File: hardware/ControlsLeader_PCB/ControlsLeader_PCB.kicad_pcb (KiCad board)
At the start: 2 copper layers, 42 parts, among them J1 CarCANConnector_Out, J15 IgnConn_01x04, J16 SteeringConn_01x05, J17 Conn_01x02, J2 PeripheralCAN_out, J3 CarCANConnector_In, J4 PeripheralCAN_in, J6 DashConn1_2Rows-09Pins, J7 Dash_LSOM_PWR, J8 DashConn2_2Rows-09Pins, Q14 NMOS, Q6 NMOS, Q9 NMOS, U2 LeaderSOM, U4 LT1963AEST-3.3#TRPBF, U6 TPS5405DR

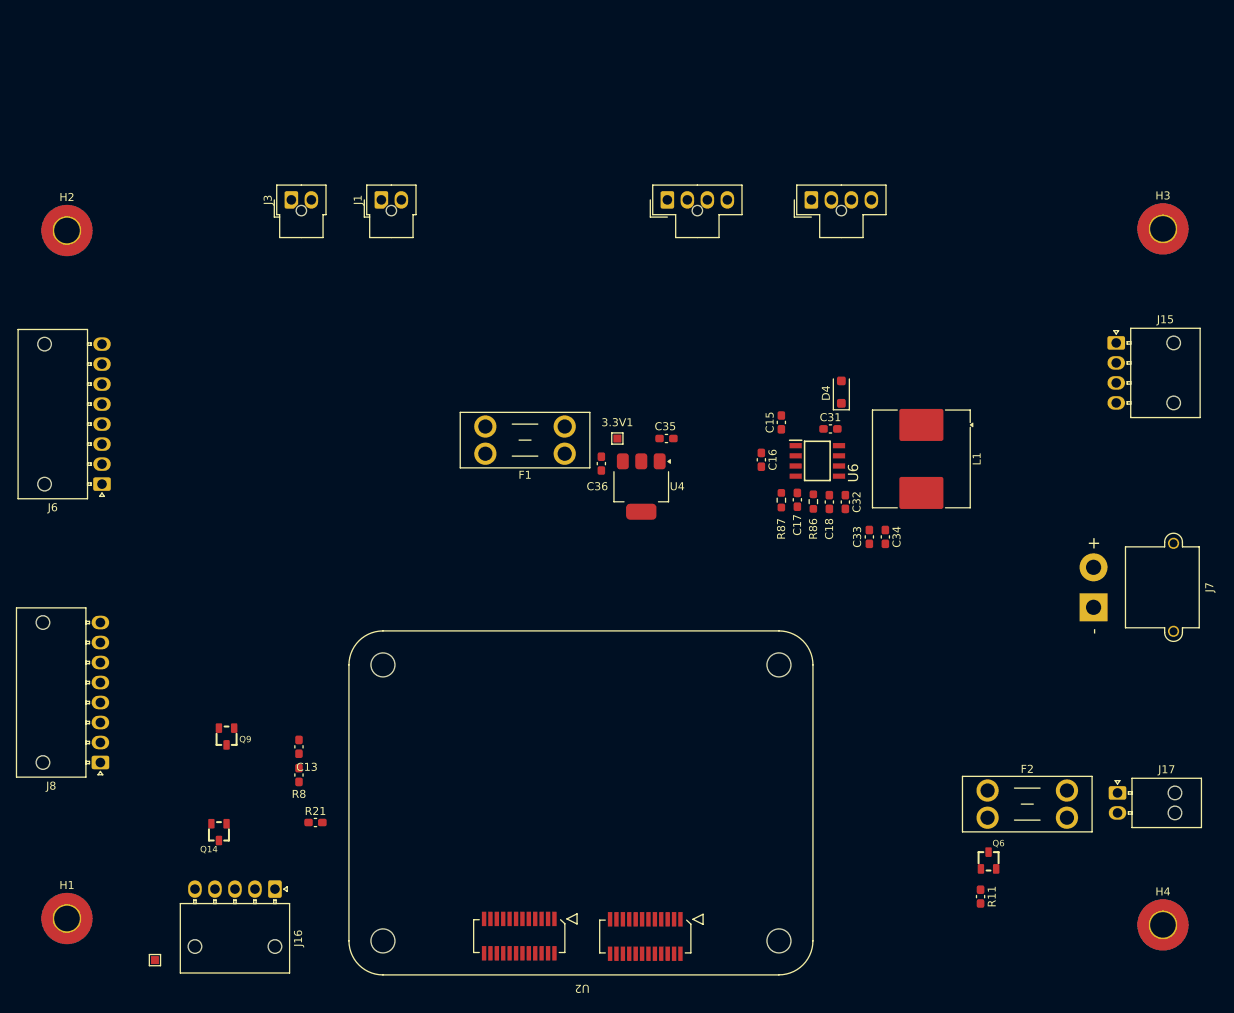
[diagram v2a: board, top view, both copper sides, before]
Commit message: PCB DESIGN DONE - need to add datasheets and p/n
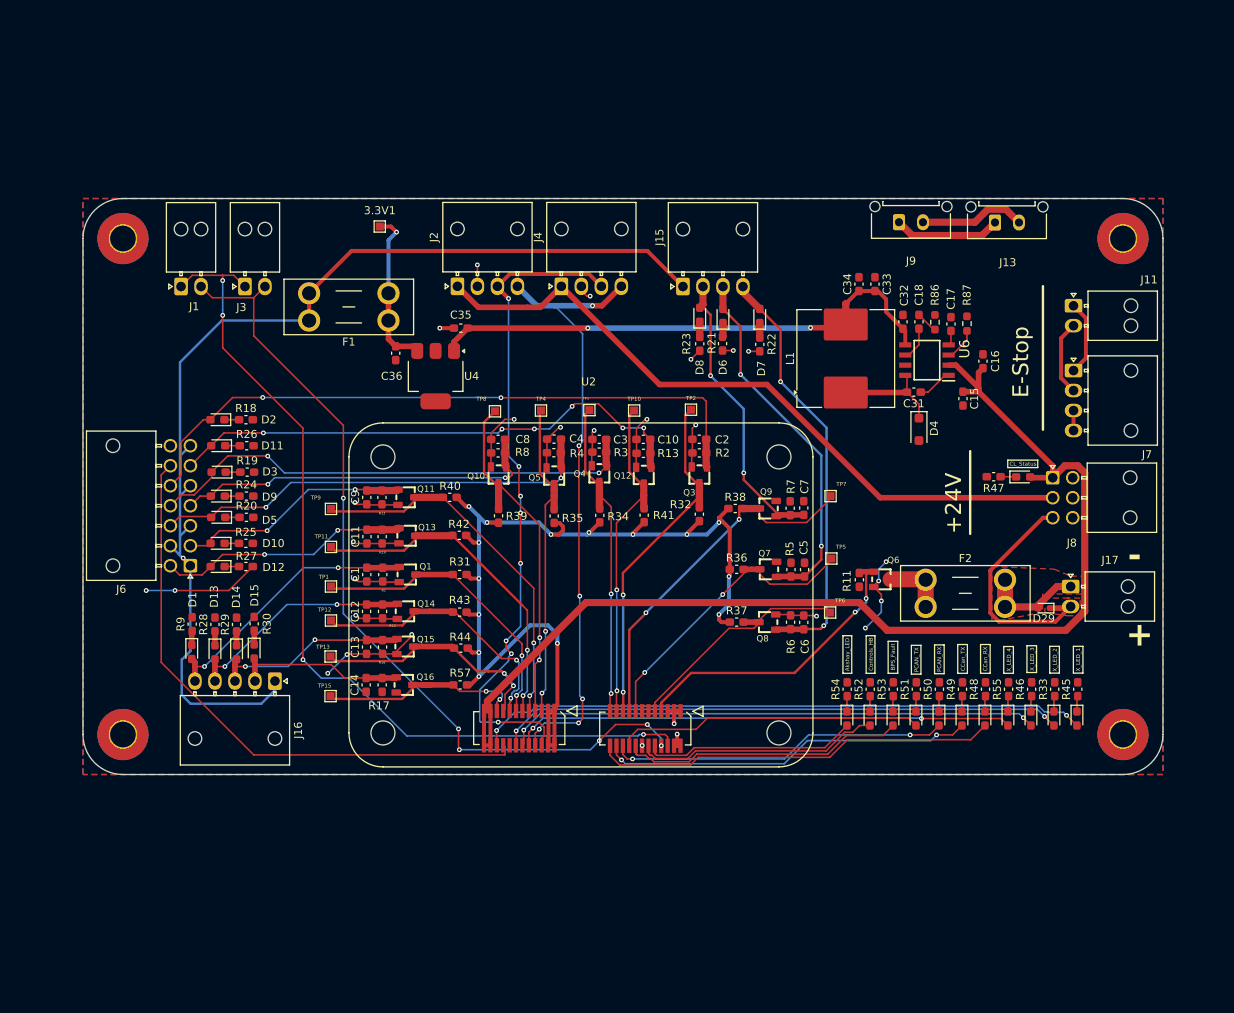
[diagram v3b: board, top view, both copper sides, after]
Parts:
- added C1: 5uF, Capacitor_SMD:C_0603_1608Metric_Pad1.08x0.95mm_HandSolder, F.Cu at (120.5, 105.0)
- added C10: 5uF, Capacitor_SMD:C_0603_1608Metric_Pad1.08x0.95mm_HandSolder, F.Cu at (155.1, 88.1)
- added C11: 5uF, Capacitor_SMD:C_0603_1608Metric_Pad1.08x0.95mm_HandSolder, F.Cu at (120.5, 100.3)
- added C12: 5uF, Capacitor_SMD:C_0603_1608Metric_Pad1.08x0.95mm_HandSolder, F.Cu at (120.5, 109.6)
- added C14: 5uF, Capacitor_SMD:C_0603_1608Metric_Pad1.08x0.95mm_HandSolder, F.Cu at (120.4, 118.8)
- added C2: 5uF, Capacitor_SMD:C_0603_1608Metric_Pad1.08x0.95mm_HandSolder, F.Cu at (162.0, 88.1)
- added C3: 5uF, Capacitor_SMD:C_0603_1608Metric_Pad1.08x0.95mm_HandSolder, F.Cu at (149.5, 88.1)
- added C4: 5uF, Capacitor_SMD:C_0603_1608Metric_Pad1.08x0.95mm_HandSolder, F.Cu at (143.9, 88.1)
- added C5: 5uF, Capacitor_SMD:C_0603_1608Metric_Pad1.08x0.95mm_HandSolder, F.Cu at (175.2, 104.4)
- added C6: 5uF, Capacitor_SMD:C_0603_1608Metric_Pad1.08x0.95mm_HandSolder, F.Cu at (175.1, 111.0)
- added C7: 5uF, Capacitor_SMD:C_0603_1608Metric_Pad1.08x0.95mm_HandSolder, F.Cu at (175.1, 96.7)
- added C8: 5uF, Capacitor_SMD:C_0603_1608Metric_Pad1.08x0.95mm_HandSolder, F.Cu at (136.9, 88.1)
- added C9: 5uF, Capacitor_SMD:C_0603_1608Metric_Pad1.08x0.95mm_HandSolder, F.Cu at (120.5, 95.4)
- added D1: GPIO_Status_Blue, LED_SMD:LED_0603_1608Metric_Pad1.05x0.95mm_HandSolder, F.Cu at (98.6, 114.7)
- added D10: GPIO_Status_Blue, LED_SMD:LED_0603_1608Metric_Pad1.05x0.95mm_HandSolder, F.Cu at (101.8, 101.1)
- added D11: GPIO_Status_Blue, LED_SMD:LED_0603_1608Metric_Pad1.05x0.95mm_HandSolder, F.Cu at (101.9, 88.9)
- added D12: GPIO_Status_Blue, LED_SMD:LED_0603_1608Metric_Pad1.05x0.95mm_HandSolder, F.Cu at (101.8, 104.0)
- added D13: GPIO_Status_Blue, LED_SMD:LED_0603_1608Metric_Pad1.05x0.95mm_HandSolder, F.Cu at (101.5, 114.7)
- added D14: GPIO_Status_Blue, LED_SMD:LED_0603_1608Metric_Pad1.05x0.95mm_HandSolder, F.Cu at (104.2, 114.7)
- added D15: GPIO_Status_Blue, LED_SMD:LED_0603_1608Metric_Pad1.05x0.95mm_HandSolder, F.Cu at (106.4, 114.6)
- added D16: Controls_Leader_Status_Red, LED_SMD:LED_0603_1608Metric_Pad1.05x0.95mm_HandSolder, F.Cu at (202.5, 92.8)
- added D17: 0603_SMD, LED_SMD:LED_0603_1608Metric_Pad1.05x0.95mm_HandSolder, F.Cu at (209.2, 123.0)
- added D18: 0603_SMD, LED_SMD:LED_0603_1608Metric_Pad1.05x0.95mm_HandSolder, F.Cu at (206.4, 123.0)
- added D19: 0603_SMD, LED_SMD:LED_0603_1608Metric_Pad1.05x0.95mm_HandSolder, F.Cu at (197.8, 123.0)
- added D2: GPIO_Status_Blue, LED_SMD:LED_0603_1608Metric_Pad1.05x0.95mm_HandSolder, F.Cu at (101.8, 85.7)
- added D20: 0603_SMD, LED_SMD:LED_0603_1608Metric_Pad1.05x0.95mm_HandSolder, F.Cu at (194.9, 123.0)
- added D21: 0603_SMD, LED_SMD:LED_0603_1608Metric_Pad1.05x0.95mm_HandSolder, F.Cu at (192.0, 123.0)
- added D22: 0603_SMD, LED_SMD:LED_0603_1608Metric_Pad1.05x0.95mm_HandSolder, F.Cu at (189.1, 123.0)
- added D23: 0603_SMD, LED_SMD:LED_0603_1608Metric_Pad1.05x0.95mm_HandSolder, F.Cu at (183.4, 123.0)
- added D24: 0603_SMD, LED_SMD:LED_0603_1608Metric_Pad1.05x0.95mm_HandSolder, F.Cu at (186.2, 123.0)
- added D25: 0603_SMD, LED_SMD:LED_0603_1608Metric_Pad1.05x0.95mm_HandSolder, F.Cu at (180.5, 123.0)
- added D26: 0603_SMD, LED_SMD:LED_0603_1608Metric_Pad1.05x0.95mm_HandSolder, F.Cu at (203.5, 123.0)
- added D27: 0603_SMD, LED_SMD:LED_0603_1608Metric_Pad1.05x0.95mm_HandSolder, F.Cu at (200.6, 123.0)
- added D29: VSSAF522-M3/H, Diode_SMD:D_SOD-523, F.Cu at (205.1, 109.2)
- added D3: GPIO_Status_Blue, LED_SMD:LED_0603_1608Metric_Pad1.05x0.95mm_HandSolder, F.Cu at (102.0, 92.2)
- added D5: GPIO_Status_Blue, LED_SMD:LED_0603_1608Metric_Pad1.05x0.95mm_HandSolder, F.Cu at (101.9, 97.8)
- added D6: GPIO_Status_Blue, LED_SMD:LED_0603_1608Metric_Pad1.05x0.95mm_HandSolder, F.Cu at (165.0, 72.7)
- added D7: GPIO_Status_Blue, LED_SMD:LED_0603_1608Metric_Pad1.05x0.95mm_HandSolder, F.Cu at (169.6, 72.7)
- added D8: GPIO_Status_Blue, LED_SMD:LED_0603_1608Metric_Pad1.05x0.95mm_HandSolder, F.Cu at (162.1, 72.5)
- added D9: GPIO_Status_Blue, LED_SMD:LED_0603_1608Metric_Pad1.05x0.95mm_HandSolder, F.Cu at (101.9, 95.2)
- added J11: EStop1, Connector_Molex:Molex_Nano-Fit_105313-xx02_1x02_P2.50mm_Horizontal, F.Cu at (208.8, 71.4)
- added J13: Supp_Out, Connector_Molex:Molex_Micro-Fit_3.0_43650-0215_1x02_P3.00mm_Vertical, F.Cu at (199.0, 61.0)
- added J9: Supp_In, Connector_Molex:Molex_Micro-Fit_3.0_43650-0215_1x02_P3.00mm_Vertical, F.Cu at (187.0, 61.0)
- added Q1: NMOS, LSOM_IRLM:SOT23, F.Cu at (124.5, 104.0)
- added Q10: NMOS, LSOM_IRLM:SOT23, F.Cu at (137.9, 91.5)
- added Q11: NMOS, LSOM_IRLM:SOT23, F.Cu at (124.4, 94.4)
- added Q12: NMOS, LSOM_IRLM:SOT23, F.Cu at (156.1, 91.6)
- added Q13: NMOS, LSOM_IRLM:SOT23, F.Cu at (124.5, 99.2)
- added Q15: NMOS, LSOM_IRLM:SOT23, F.Cu at (124.2, 113.0)
- added Q16: NMOS, LSOM_IRLM:SOT23, F.Cu at (124.2, 117.8)
- added Q3: NMOS, LSOM_IRLM:SOT23, F.Cu at (163.0, 91.5)
- added Q4: NMOS, LSOM_IRLM:SOT23, F.Cu at (150.5, 91.4)
- added Q5: NMOS, LSOM_IRLM:SOT23, F.Cu at (144.8, 91.7)
- added Q7: NMOS, LSOM_IRLM:SOT23, F.Cu at (171.7, 105.3)
- added Q8: NMOS, LSOM_IRLM:SOT23, F.Cu at (171.6, 111.9)
- added R1: 10k, Capacitor_SMD:C_0603_1608Metric_Pad1.08x0.95mm_HandSolder, F.Cu at (122.5, 105.0)
- added R12: 10k, Capacitor_SMD:C_0603_1608Metric_Pad1.08x0.95mm_HandSolder, F.Cu at (122.4, 95.4)
- added R13: 10k, Capacitor_SMD:C_0603_1608Metric_Pad1.08x0.95mm_HandSolder, F.Cu at (155.1, 89.8)
- added R14: 10k, Capacitor_SMD:C_0603_1608Metric_Pad1.08x0.95mm_HandSolder, F.Cu at (122.4, 100.3)
- added R15: 10k, Capacitor_SMD:C_0603_1608Metric_Pad1.08x0.95mm_HandSolder, F.Cu at (122.5, 109.6)
- added R16: 10k, Capacitor_SMD:C_0603_1608Metric_Pad1.08x0.95mm_HandSolder, F.Cu at (122.5, 114.1)
- added R17: 10k, Capacitor_SMD:C_0603_1608Metric_Pad1.08x0.95mm_HandSolder, F.Cu at (122.4, 118.8)
- added R18: 150, Capacitor_SMD:C_0603_1608Metric_Pad1.08x0.95mm_HandSolder, F.Cu at (105.4, 85.7)
- added R19: 150, Capacitor_SMD:C_0603_1608Metric_Pad1.08x0.95mm_HandSolder, F.Cu at (105.5, 92.2)
- added R2: 10k, Capacitor_SMD:C_0603_1608Metric_Pad1.08x0.95mm_HandSolder, F.Cu at (162.1, 89.8)
- added R20: 150, Capacitor_SMD:C_0603_1608Metric_Pad1.08x0.95mm_HandSolder, F.Cu at (105.4, 97.8)
- added R22: 150, Capacitor_SMD:C_0603_1608Metric_Pad1.08x0.95mm_HandSolder, F.Cu at (169.6, 76.2)
- added R23: 150, Capacitor_SMD:C_0603_1608Metric_Pad1.08x0.95mm_HandSolder, F.Cu at (162.1, 76.2)
- added R24: 150, Capacitor_SMD:C_0603_1608Metric_Pad1.08x0.95mm_HandSolder, F.Cu at (105.4, 95.2)
- added R25: 150, Capacitor_SMD:C_0603_1608Metric_Pad1.08x0.95mm_HandSolder, F.Cu at (105.4, 101.1)
- added R26: 150, Capacitor_SMD:C_0603_1608Metric_Pad1.08x0.95mm_HandSolder, F.Cu at (105.5, 88.9)
- added R27: 150, Capacitor_SMD:C_0603_1608Metric_Pad1.08x0.95mm_HandSolder, F.Cu at (105.4, 104.0)
- added R28: 150, Capacitor_SMD:C_0603_1608Metric_Pad1.08x0.95mm_HandSolder, F.Cu at (101.5, 111.2)
- added R29: 150, Capacitor_SMD:C_0603_1608Metric_Pad1.08x0.95mm_HandSolder, F.Cu at (104.2, 111.2)
- added R3: 10k, Capacitor_SMD:C_0603_1608Metric_Pad1.08x0.95mm_HandSolder, F.Cu at (149.5, 89.7)
- added R30: 150, Capacitor_SMD:C_0603_1608Metric_Pad1.08x0.95mm_HandSolder, F.Cu at (106.4, 111.2)
- added R31: 100k, Capacitor_SMD:C_0603_1608Metric_Pad1.08x0.95mm_HandSolder, F.Cu at (132.1, 105.0)
- added R32: 100k, Capacitor_SMD:C_0603_1608Metric_Pad1.08x0.95mm_HandSolder, F.Cu at (162.1, 97.5)
- added R33: 65, Capacitor_SMD:C_0603_1608Metric_Pad1.08x0.95mm_HandSolder, F.Cu at (206.5, 119.3)
- added R34: 100k, Capacitor_SMD:C_0603_1608Metric_Pad1.08x0.95mm_HandSolder, F.Cu at (149.6, 97.6)
- added R35: 100k, Capacitor_SMD:C_0603_1608Metric_Pad1.08x0.95mm_HandSolder, F.Cu at (143.9, 97.7)
- added R36: 100k, Capacitor_SMD:C_0603_1608Metric_Pad1.08x0.95mm_HandSolder, F.Cu at (166.7, 104.3)
- added R37: 100k, Capacitor_SMD:C_0603_1608Metric_Pad1.08x0.95mm_HandSolder, F.Cu at (166.7, 111.0)
- added R38: 100k, Capacitor_SMD:C_0603_1608Metric_Pad1.08x0.95mm_HandSolder, F.Cu at (166.5, 96.8)
- added R39: 100k, Capacitor_SMD:C_0603_1608Metric_Pad1.08x0.95mm_HandSolder, F.Cu at (136.9, 97.7)
- added R4: 10k, Capacitor_SMD:C_0603_1608Metric_Pad1.08x0.95mm_HandSolder, F.Cu at (143.9, 89.8)
- added R40: 100k, Capacitor_SMD:C_0603_1608Metric_Pad1.08x0.95mm_HandSolder, F.Cu at (130.8, 95.3)
- added R41: 100k, Capacitor_SMD:C_0603_1608Metric_Pad1.08x0.95mm_HandSolder, F.Cu at (155.2, 97.6)
- added R42: 100k, Capacitor_SMD:C_0603_1608Metric_Pad1.08x0.95mm_HandSolder, F.Cu at (132.0, 100.1)
- added R43: 100k, Capacitor_SMD:C_0603_1608Metric_Pad1.08x0.95mm_HandSolder, F.Cu at (132.1, 109.7)
- added R44: 100k, Capacitor_SMD:C_0603_1608Metric_Pad1.08x0.95mm_HandSolder, F.Cu at (132.2, 114.2)
- added R45: 65, Capacitor_SMD:C_0603_1608Metric_Pad1.08x0.95mm_HandSolder, F.Cu at (209.3, 119.3)
- added R46: 65, Capacitor_SMD:C_0603_1608Metric_Pad1.08x0.95mm_HandSolder, F.Cu at (203.6, 119.3)
- added R47: 1.1k, Capacitor_SMD:C_0603_1608Metric_Pad1.08x0.95mm_HandSolder, F.Cu at (198.8, 92.8)
- added R48: 20, Capacitor_SMD:C_0603_1608Metric_Pad1.08x0.95mm_HandSolder, F.Cu at (197.8, 119.3)
- added R49: 20, Capacitor_SMD:C_0603_1608Metric_Pad1.08x0.95mm_HandSolder, F.Cu at (194.9, 119.3)
- added R5: 10k, Capacitor_SMD:C_0603_1608Metric_Pad1.08x0.95mm_HandSolder, F.Cu at (173.5, 104.4)
- added R50: 20, Capacitor_SMD:C_0603_1608Metric_Pad1.08x0.95mm_HandSolder, F.Cu at (192.1, 119.3)
- added R51: 20, Capacitor_SMD:C_0603_1608Metric_Pad1.08x0.95mm_HandSolder, F.Cu at (189.2, 119.3)
- added R52: 20, Capacitor_SMD:C_0603_1608Metric_Pad1.08x0.95mm_HandSolder, F.Cu at (183.4, 119.3)
- added R53: 20, Capacitor_SMD:C_0603_1608Metric_Pad1.08x0.95mm_HandSolder, F.Cu at (186.3, 119.3)
- added R54: 20, Capacitor_SMD:C_0603_1608Metric_Pad1.08x0.95mm_HandSolder, F.Cu at (180.5, 119.3)
- added R55: 65, Capacitor_SMD:C_0603_1608Metric_Pad1.08x0.95mm_HandSolder, F.Cu at (200.7, 119.3)
- added R57: 100k, Capacitor_SMD:C_0603_1608Metric_Pad1.08x0.95mm_HandSolder, F.Cu at (132.2, 118.8)
- added R6: 10k, Capacitor_SMD:C_0603_1608Metric_Pad1.08x0.95mm_HandSolder, F.Cu at (173.4, 111.0)
- added R7: 10k, Capacitor_SMD:C_0603_1608Metric_Pad1.08x0.95mm_HandSolder, F.Cu at (173.4, 96.7)
- added R9: 150, Capacitor_SMD:C_0603_1608Metric_Pad1.08x0.95mm_HandSolder, F.Cu at (98.7, 111.2)
- added TP1: TestPoint, TestPoint:TestPoint_Pad_1.0x1.0mm, F.Cu at (116.0, 106.5)
- added TP10: TestPoint, TestPoint:TestPoint_Pad_1.0x1.0mm, F.Cu at (153.9, 84.5)
- added TP11: TestPoint, TestPoint:TestPoint_Pad_1.0x1.0mm, F.Cu at (116.0, 101.5)
- added TP12: TestPoint, TestPoint:TestPoint_Pad_1.0x1.0mm, F.Cu at (116.0, 110.8)
- added TP15: TestPoint, TestPoint:TestPoint_Pad_1.0x1.0mm, F.Cu at (116.0, 120.2)
- added TP2: TestPoint, TestPoint:TestPoint_Pad_1.0x1.0mm, F.Cu at (161.0, 84.4)
- added TP3: TestPoint, TestPoint:TestPoint_Pad_1.0x1.0mm, F.Cu at (148.3, 84.5)
- added TP4: TestPoint, TestPoint:TestPoint_Pad_1.0x1.0mm, F.Cu at (142.2, 84.5)
- added TP5: TestPoint, TestPoint:TestPoint_Pad_1.0x1.0mm, F.Cu at (178.6, 103.0)
- added TP6: TestPoint, TestPoint:TestPoint_Pad_1.0x1.0mm, F.Cu at (178.4, 109.8)
- added TP7: TestPoint, TestPoint:TestPoint_Pad_1.0x1.0mm, F.Cu at (178.4, 95.2)
- added TP8: TestPoint, TestPoint:TestPoint_Pad_1.0x1.0mm, F.Cu at (136.5, 84.6)
- added TP9: TestPoint, TestPoint:TestPoint_Pad_1.0x1.0mm, F.Cu at (116.0, 96.8)
- J1, J3: footprint UTSVT_Connectors:Molex_Nano-Fit_105309-xx02_1x02_P2.50mm_Vertical -> Connector_Molex:Molex_Nano-Fit_105313-xx02_1x02_P2.50mm_Horizontal
- J2, J4: footprint UTSVT_Connectors:Molex_Nano-Fit_105309-xx04_1x04_P2.50mm_Vertical -> Connector_Molex:Molex_Nano-Fit_105313-xx04_1x04_P2.50mm_Horizontal
- J6: value DashConn1_2Rows-09Pins -> Conn_2Rows-13Pins; footprint Connector_Molex:Molex_Nano-Fit_105313-xx08_1x08_P2.50mm_Horizontal -> Connector_Molex:Molex_Nano-Fit_105314-xx14_2x07_P2.50mm_Horizontal
- J7: value Dash_LSOM_PWR -> Conn_01x04; footprint UTSVT_Connectors:AMASS_XT30PW-M_1x02_P2.50mm_Horizontal -> Connector_Molex:Molex_Nano-Fit_105313-xx04_1x04_P2.50mm_Horizontal
- J8: value DashConn2_2Rows-09Pins -> Dash_Lsom_Horn_Lights_PWR; footprint Connector_Molex:Molex_Nano-Fit_105313-xx08_1x08_P2.50mm_Horizontal -> Connector_Molex:Molex_Nano-Fit_105314-xx06_2x03_P2.50mm_Horizontal
- moved H4 132.2 mm to (90.0, 125.0)
- moved H2 132.0 mm to (215.0, 63.0)
- moved J8 124.2 mm to (206.2, 92.9), turned to 0 degrees
- moved H1 85.3 mm to (90.0, 63.0)
- moved R21 78.6 mm to (164.9, 76.1), turned to -90 degrees
- moved Q9 72.7 mm to (171.7, 97.7), turned to 90 degrees
- moved H3 63.4 mm to (215.0, 125.0)
- moved J15 54.6 mm to (160.0, 69.0), turned to 90 degrees
- moved J2 48.5 mm to (131.8, 69.0)
- moved R8 47.3 mm to (136.9, 89.8), turned to 0 degrees
- moved TP13 43.8 mm to (116.0, 115.2)
- moved R11 42.4 mm to (182.1, 105.7)
- moved 3.3V1 39.8 mm to (122.1, 61.5)
- moved Q6 39.5 mm to (183.8, 104.7), turned to -90 degrees
- moved Q14 34.8 mm to (124.3, 108.7), turned to -90 degrees
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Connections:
- C13 pad 2: /Steering_Wheel/NMOS Switch1/3.3V_LDO_Switch -> /Right_Blinker_Signal
- J15 pad 2: /Ign_mtr_GPIO -> /Ign_mtr_Signal
- J15 pad 3: /Ign_OFF_GPIO -> /Ign_off_Signal
- J15 pad 4: /Ign_arr_GPIO -> /Ign_arr_Signal
- J16 pad 2: /Left_Blinker_ON -> /Left_Blinker_Signal
- J16 pad 3: /Right_Blinker_ON -> /Right_Blinker_Signal
- J16 pad 4: /Horn_GPIO_IN -> /Horn_3.3V_Signal
- J16 pad 5: /Regen_Active_GPIO_IN -> /Regen_Active_Signal
- J17 pad 2: unconnected-(J17-Pin_2-Pad2) -> /+24v_Horn
- J2 pad 1: +24V -> /+24v_Lights
- J4 pad 1: +24V -> /+24v_Lights
- J6 pad 2: /Rev_SW_GPIO -> /Cruise_Set_Signal
- J6 pad 4: /Fwd_SW_GPIO -> /Cruise_Enable_Signal
- J6 pad 6: /Neutral_Gear_GPIO -> /Regen_Enable_Signal
- J6 pad 8: unconnected-(J6-Pin_8-Pad8) -> /Hazard_Signal
- J7 pad 1: +24V -> /Dash/Contactor_OUT1
- J7 pad 2: GND -> /Dash/Contactor_IN1
- J8 pad 1: /3.3V_LDO -> +24V
- J8 pad 2: /Cruise_Set_GPIO_IN -> /+24v_Lights
- J8 pad 3: /3.3V_LDO -> /+24v_Horn
- J8 pad 4: /Cruise_Enable_GPIO_IN -> GND
- J8 pad 5: /3.3V_LDO -> GND
- J8 pad 6: /Regen_Enable_GPIO_IN -> GND
- Q14 pad 2: /Steering_Wheel/NMOS Switch3/3.3V_LDO_Switch -> /Horn_3.3V_Signal
- Q9 pad 2: /Dash/NMOS Switch5/3.3V_LDO_Switch -> /Ign_mtr_Signal
- R8 pad 2: /Dash/NMOS Switch6/3.3V_LDO_Switch -> /Cruise_Enable_Signal
- U2 pad 10: /Extra_LED1 -> /Extra_LED4
- U2 pad 11: /Horn_24V_Signal_Out -> /Hazard_GPIO_IN
- U2 pad 12: /Extra_LED2 -> /Extra_LED3
- U2 pad 13: /Extra_LED3 -> /Regen_Active_GPIO_IN
- U2 pad 14: /PH_Can_TX_LED -> /Extra_LED2
- U2 pad 15: /Akshay_LED -> /Horn_GPIO_IN
- U2 pad 17: /BPS_Fault_LED -> /Right_Blinker_ON
- U2 pad 18: /Extra_LED5 -> /Indicator_PWM
- U2 pad 19: /CarCan_RX_LED -> /Left_Blinker_ON
- U2 pad 20: /Extra_LED4 -> /Extra_LED1
- U2 pad 31: /Regen_Active_GPIO_IN -> /Horn_GPIO_OUT
- U2 pad 33: /Indicator_PWM -> /Ign_arr_GPIO
- U2 pad 34: /Ign_OFF_GPIO -> /Akshay_LED
- U2 pad 36: /Neutral_Gear_GPIO -> /Controls_HB_LED
- U2 pad 39: /Right_Blinker_ON -> /Ign_OFF_GPIO
- U2 pad 40: /Left_Blinker_ON -> /BPS_Fault_LED
- U2 pad 41: /Hazard_GPIO_IN -> /Ign_mtr_GPIO
- U2 pad 42: /Rev_SW_GPIO -> /PH_Can_TX_LED
- U2 pad 43: /Regen_Enable_GPIO_IN -> /Fwd_SW_GPIO
- U2 pad 44: /Fwd_SW_GPIO -> /PH_Can_RX_LED
- U2 pad 45: /Cruise_Enable_GPIO_IN -> /Regen_Enable_GPIO_IN
- U2 pad 46: /Ign_mtr_GPIO -> /CarCan_TX_LED
- U2 pad 47: /Cruise_Set_GPIO_IN -> /Neutral_Gear_GPIO
- U2 pad 48: /Ign_arr_GPIO -> /CarCan_RX_LED
- U2 pad 5: /CarCan_TX_LED -> /Rev_SW_GPIO
- U2 pad 7: /Controls_HB_LED -> /Cruise_Enable_GPIO_IN
- U2 pad 9: /PH_Can_RX_LED -> /Cruise_Set_GPIO_IN
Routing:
- net +24V: track 0.00 -> 143.9 mm
- net /3.3V_LDO: track 0.00 -> 136.3 mm, vias 0 -> 1
- net /3.3V_LSOM: track 0.00 -> 129.5 mm, vias 0 -> 15
- net /CarCan_H: track 0.00 -> 112.4 mm, vias 0 -> 4
- net GND: track 0.00 -> 112.0 mm, vias 0 -> 28
- net /CarCan_L: track 0.00 -> 104.6 mm, vias 0 -> 6
- net /+24v_Lights: track 0.00 -> 87.5 mm
- net /PerCan_H: track 0.00 -> 83.2 mm, vias 0 -> 8
- net /Fwd_SW_Signal: track 0.00 -> 82.4 mm, vias 0 -> 2
- net /PerCan_L: track 0.00 -> 76.7 mm, vias 0 -> 6
- net /Extra_LED1: track 0.00 -> 76.7 mm, vias 0 -> 2
- net /Indicator_PWM: track 0.00 -> 74.1 mm
- net /Extra_LED2: track 0.00 -> 71.0 mm, vias 0 -> 2
- net /Extra_LED3: track 0.00 -> 66.8 mm, vias 0 -> 2
- net /Regen_Enable_Signal: track 0.00 -> 66.5 mm, vias 0 -> 6
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- added copper zone on F.Cu, net /+24v_Horn
- added copper zone on F.Cu, net /Horn_24V_Signal_Out
- added copper zone on B.Cu, net GND
- added copper zone on F.Cu, net GND
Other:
- board outline added: 135 x 72 mm
- board text added: "+"
- board text added: "+24V"
- board text added: "-"
- board text added: "Akshay_LED"
- board text added: "BPS_Fault"
- board text added: "CCan_RX"
- board text added: "CCan_TX"
- board text added: "CL_Status"
- board text added: "Controls_HB"
- board text added: "E-Stop"
- board text added: "PCAN_RX"
- board text added: "PCAN_TX"
- board text added: "X_LED_1"
- board text added: "X_LED_2"
- board text added: "X_LED_3"
- board text added: "X_LED_4"

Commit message: Updated GPIO table, addressed lakshay review
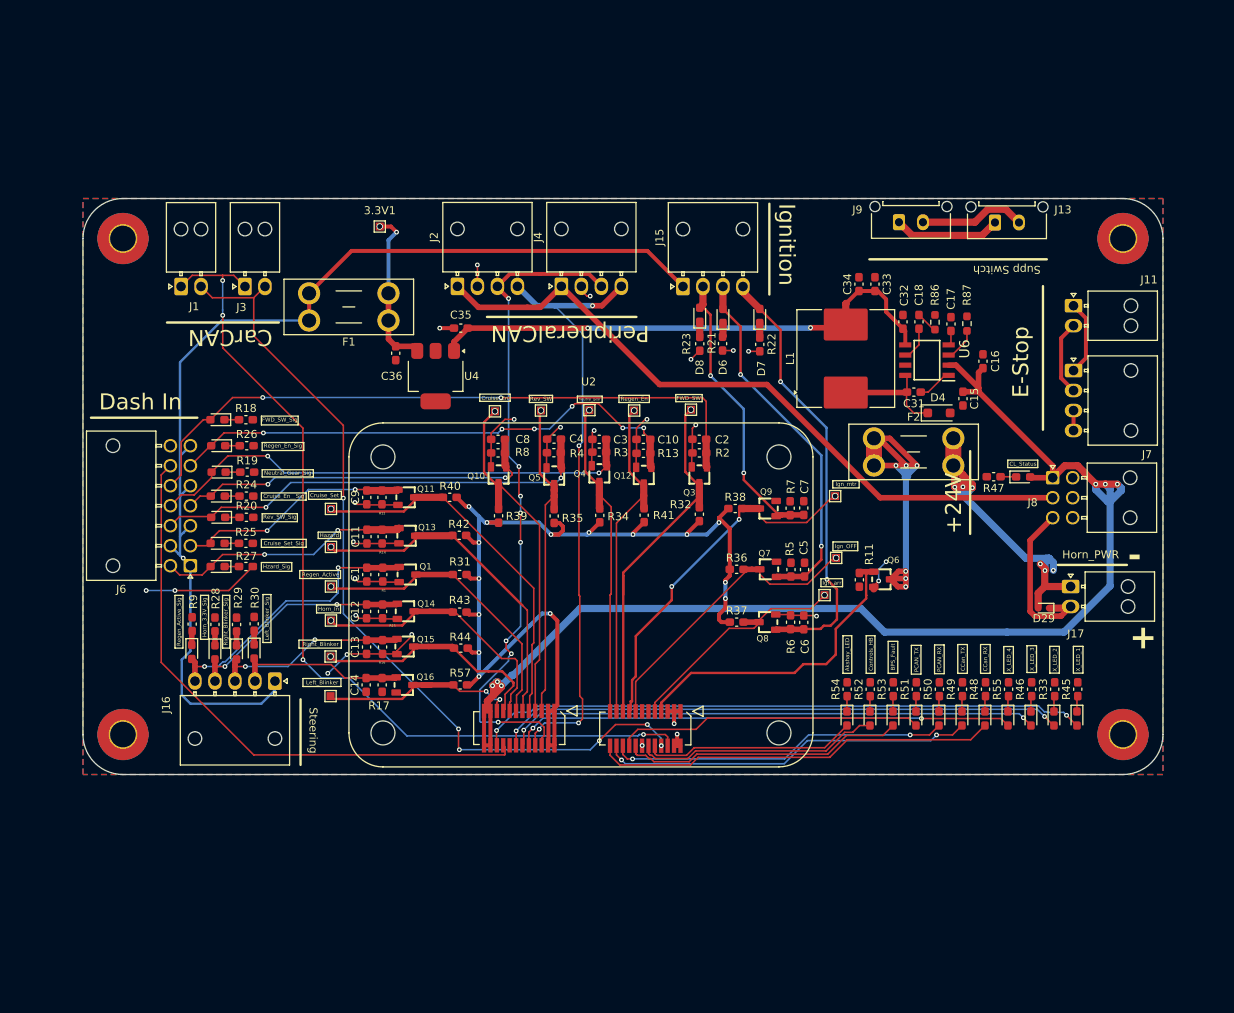
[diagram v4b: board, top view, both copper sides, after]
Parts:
- moved F2 18.8 mm to (183.9, 88.0)
- moved D4 3.23 mm to (192.0, 84.8), turned to 0 degrees
- moved Ign_arr 2.28 mm to (177.7, 107.6)
- moved Ign_OFF 0.60 mm to (179.2, 102.9)
- moved Ign_mtr 0.58 mm to (179.0, 95.2)
- renumbered TP8 to Cruise_En, D9 to Cruise_En__Sig, TP9 to Cruise_Set, D10 to Cruise_Set_Sig, TP2 to FWD_SW, D2 to FWD_SW_Sig, TP11 to Hazard, D13 to Horn_3.3V_Sig, TP12 to Horn_In, D12 to Hzard_Sig, TP5 to Ign_OFF, TP6 to Ign_arr, TP7 to Ign_mtr, TP15 to Left_Blinker, D15 to Left_Blinker_Sig, D3 to Neutral_Gear_Sig, TP3 to Neutral_gear, TP1 to Regen_Active, D1 to Regen_Active_Sig, TP10 to Regen_En, D11 to Regen_En_Sig, TP4 to Rev_SW, D5 to Rev_SW_Sig, TP13 to Right_Blinker, D14 to Right_Blinker_Sig
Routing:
- net Net-(Q6-D): track 7.81 -> 61.3 mm, vias 0 -> 6
- net /Horn_24V_Signal_Out: track 13.0 -> 47.6 mm, vias 0 -> 6
- net +24V: track 143.9 -> 160.2 mm, vias 0 -> 6
- net /+24v_Horn: track 30.7 -> 22.2 mm
- net GND: track 112.0 -> 105.9 mm, vias 28 -> 26
- net /Fwd_SW_GPIO: track 44.2 -> 46.6 mm, vias 2 -> 1
- net /3.3V_LSOM: track 129.5 -> 131.8 mm
- net /Regen_Active_Signal: track 33.6 -> 35.5 mm
- net /Horn_GPIO_OUT: track 37.6 -> 39.2 mm, vias 2 -> 0
- net /Ign_arr_Signal: track 53.1 -> 54.7 mm
- net /Left_Blinker_ON: track 26.4 -> 25.6 mm
- net Net-(D4-K): track 13.7 -> 14.5 mm
- net /Ign_mtr_GPIO: track 45.0 -> 45.6 mm, vias 2 -> 3
- net /Ign_OFF_GPIO: track 37.6 -> 38.1 mm, vias 2 -> 1
- net /Horn_GPIO_IN: track 34.0 -> 33.6 mm, vias 2 -> 1
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- removed copper zone on F.Cu, net /+24v_Horn
- removed copper zone on F.Cu, net /Horn_24V_Signal_Out
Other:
- board text added: "CarCAN"
- board text added: "Dash In"
- board text added: "Horn_PWR"
- board text added: "Ignition"
- board text added: "PeripheralCAN"
- board text added: "Steering"
- board text added: "Supp Switch"
